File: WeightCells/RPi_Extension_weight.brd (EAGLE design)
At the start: 80 x 50 mm, 29 parts, among them U1 AD7730BRUZ, U2 AD7730BRUZ, U3 AD7730BRUZ, U4 AD7730BRUZ, U5 AD7730BRUZ, U6 AD7730BRUZ, U7 AD7730BRUZ, U8 AD7730BRUZ, U9 STM32F103RCT6

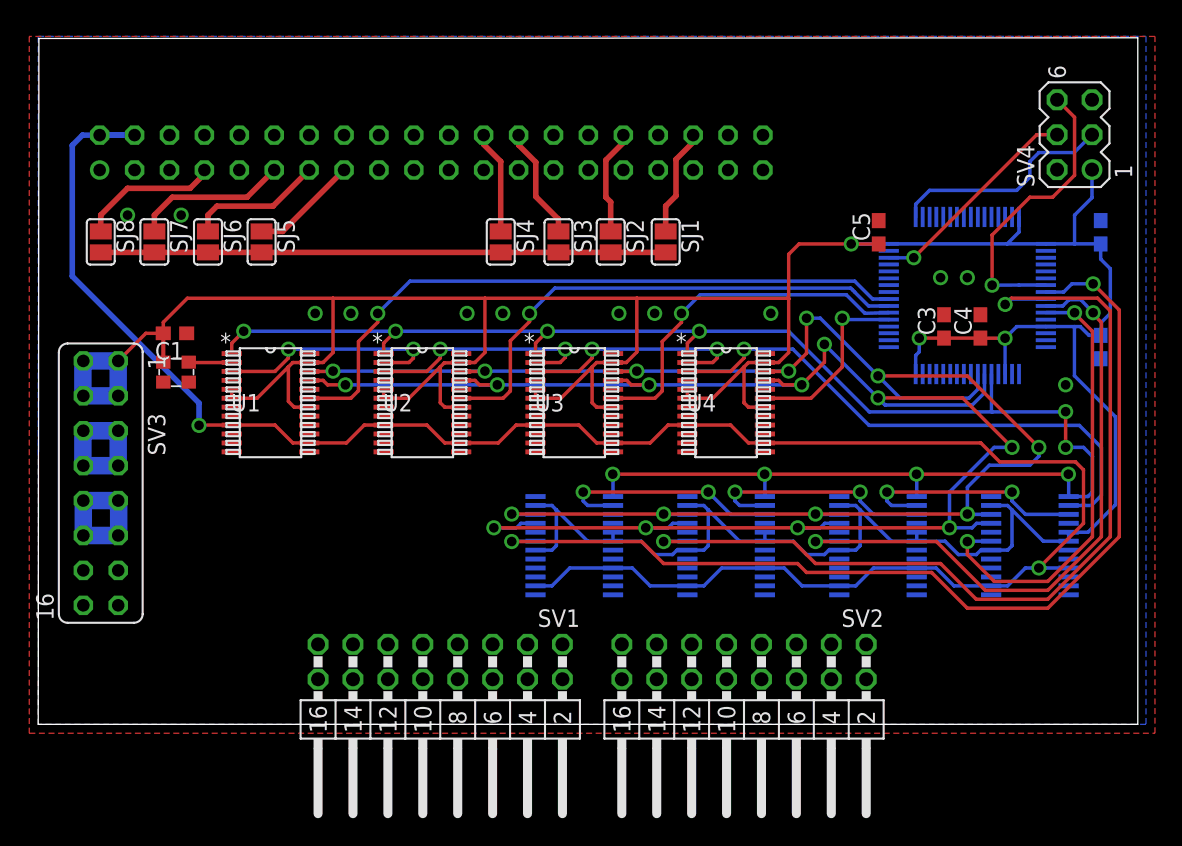
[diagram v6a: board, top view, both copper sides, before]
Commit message: shifted top ics and rerouted some signals for compliance
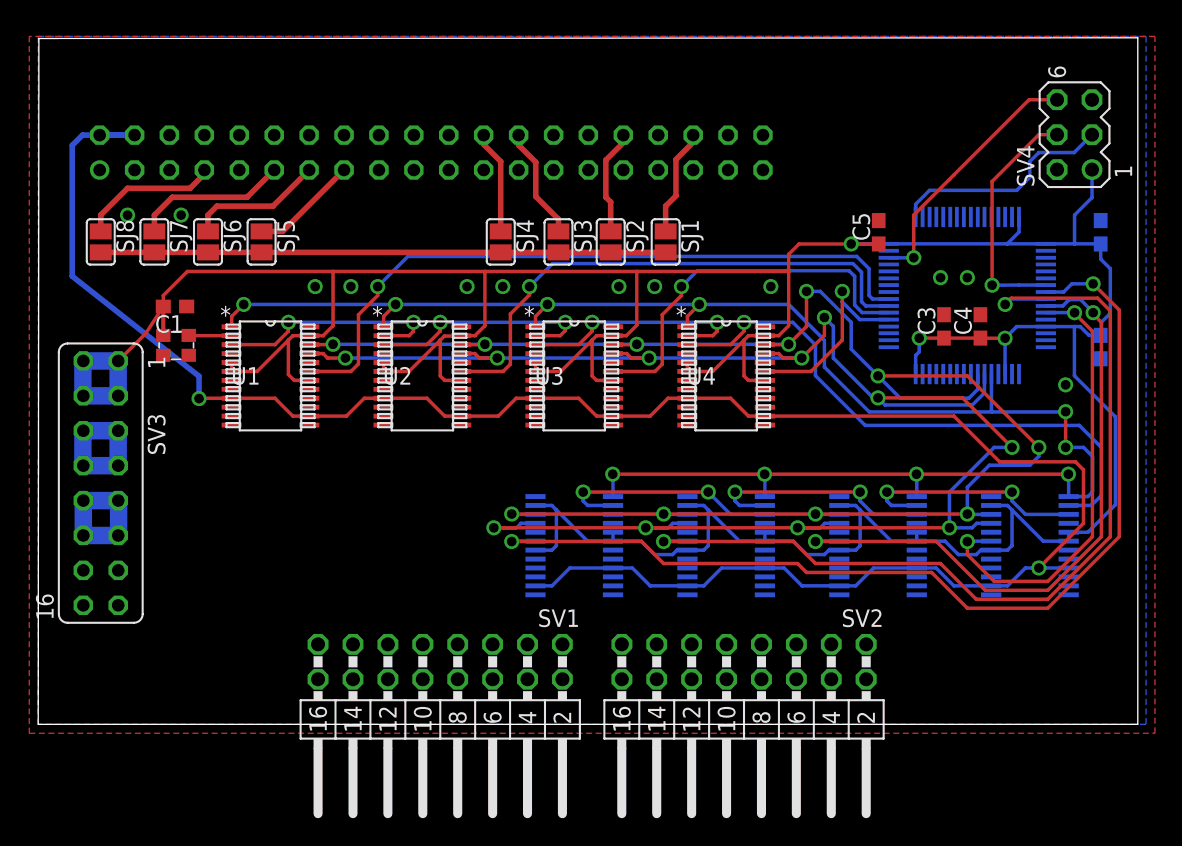
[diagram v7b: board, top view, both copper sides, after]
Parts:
- moved U1 1.95 mm to (16.9, 25.4)
- moved U2 1.95 mm to (27.9, 25.4)
- moved U3 1.95 mm to (39.0, 25.4)
- moved U4 1.95 mm to (50.0, 25.4)
- moved C1 1.95 mm to (9.95, 30.4)
- moved U$1 1.95 mm to (9.10, 28.3)
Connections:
- net NRST: now also SV4.4; no longer SV4.6
- net SWDIO: now also SV4.6; no longer SV4.4
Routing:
- net NRST: track 21.4 -> 17.6 mm
- net SWDIO: track 16.0 -> 18.8 mm
- net U4_MCLK_OUT: track 40.3 -> 42.4 mm
- net SPI1_SCK: track 121.9 -> 123.9 mm
- net SPI1_MOSI: track 123.4 -> 125.4 mm
- net SS2: track 37.5 -> 39.4 mm
- net SS3: track 26.2 -> 28.1 mm
- net SS1: track 48.7 -> 50.5 mm
- net SPI1_MISO: track 129.4 -> 130.9 mm
- net SS4: track 13.6 -> 14.8 mm
- net DVCC: track 281.8 -> 280.9 mm

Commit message: added traces to load cell connectors
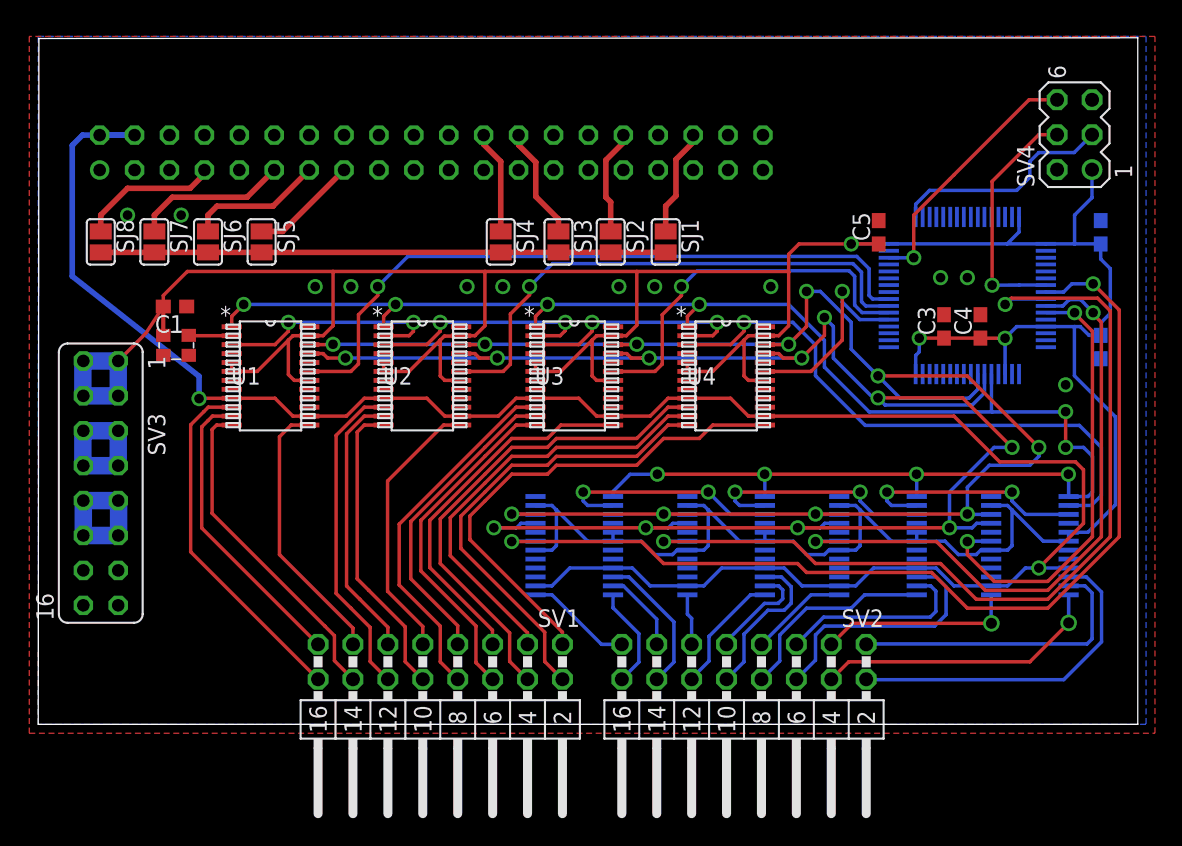
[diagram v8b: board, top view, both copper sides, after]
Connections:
- removed net N$1: U1.11
- removed net N$10: U3.10
- removed net N$11: U3.12
- removed net N$12: U3.13
- removed net N$13: U4.11
- removed net N$14: U4.10
- removed net N$15: U4.12
- removed net N$16: U4.13
- removed net N$2: U1.10
- removed net N$3: U1.12
- removed net N$4: U1.13
- removed net N$5: U2.11
- removed net N$6: U2.10
- removed net N$7: U2.12
- removed net N$8: U2.13
- removed net N$9: U3.11
- new net U5_AIN1_+: SV2.2, U5.10
- new net U5_AIN1_-: SV2.1, U5.11
- new net U5_AIN2_+: SV2.4, U5.12
- new net U5_AIN2_-: SV2.3, U5.13
- new net U6_AIN1_+: SV2.6, U6.10
- new net U6_AIN1_-: SV2.5, U6.11
- new net U6_AIN2_+: SV2.8, U6.12
- new net U6_AIN2_-: SV2.7, U6.13
- new net U7_AIN1_+: SV2.10, U7.10
- new net U7_AIN1_-: SV2.9, U7.11
- new net U7_AIN2_+: SV2.12, U7.12
- new net U7_AIN2_-: SV2.11, U7.13
- new net U8_AIN1_+: SV2.14, U8.10
- new net U8_AIN1_-: SV2.13, U8.11
- new net U8_AIN2_+: SV2.16, U8.12
- new net U8_AIN2_-: SV2.15, U8.13
- net U1_AIN1_+: now also U1.10
- net U1_AIN1_-: now also U1.11
- net U1_AIN2_+: now also U1.12
- net U1_AIN2_-: now also U1.13
- net U2_AIN1_+: now also U2.10
- net U2_AIN1_-: now also U2.11
- net U2_AIN2_+: now also U2.12
- net U2_AIN2_-: now also U2.13
- net U3_AIN1_+: now also U3.10
- net U3_AIN1_-: now also U3.11
- net U3_AIN2_+: now also U3.12
- net U3_AIN2_-: now also U3.13
- net U4_AIN1_+: now also U4.10
- net U4_AIN1_-: now also U4.11
- net U4_AIN2_+: now also U4.12
- net U4_AIN2_-: now also U4.13
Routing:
- net U4_AIN2_-: track 0.00 -> 36.3 mm
- net U4_AIN1_+: track 0.00 -> 35.6 mm
- net U4_AIN2_+: track 0.00 -> 34.2 mm
- net U4_AIN1_-: track 0.00 -> 31.9 mm
- net U3_AIN2_-: track 0.00 -> 27.1 mm
- net U3_AIN1_+: track 0.00 -> 26.5 mm
- net U1_AIN1_+: track 0.00 -> 25.9 mm
- net U3_AIN2_+: track 0.00 -> 24.9 mm
- net U5_AIN1_+: track 0.00 -> 24.7 mm
- net U1_AIN2_+: track 0.00 -> 24.0 mm
- net U2_AIN1_+: track 0.00 -> 23.6 mm
- net U3_AIN1_-: track 0.00 -> 22.6 mm
- net U2_AIN2_+: track 0.00 -> 22.1 mm
- net U5_AIN1_-: track 0.00 -> 21.9 mm
- net U1_AIN1_-: track 0.00 -> 21.8 mm
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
